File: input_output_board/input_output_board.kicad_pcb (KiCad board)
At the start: 2 copper layers, 150 x 50 mm, 24 parts, among them J1 Neutrik_NCJ6FA-H-0, J2 Neutrik_NCJ6FA-H-0, J3 Neutrik_NCJ6FA-H-0, J4 Neutrik_NCJ6FA-H-0, J5 Neutrik_NC3MAH, J6 Conn_02x05_Odd_Even, J7 Molex_SL_01x02_Male, J8 Molex_SL_01x02_Male, J9 Molex_SL_01x02_Male, K1 G6S-2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

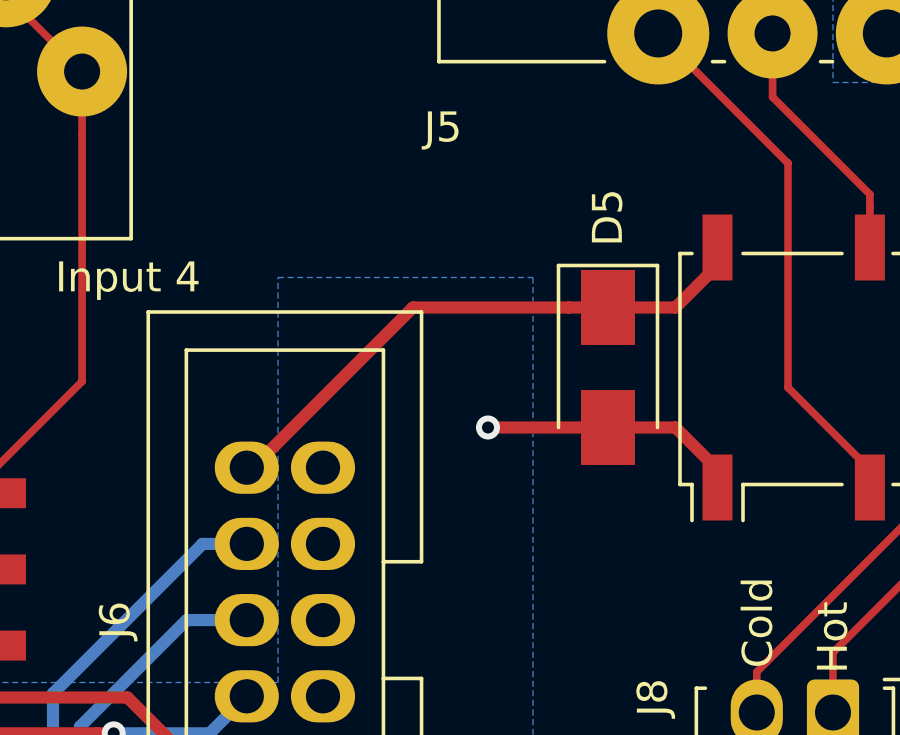
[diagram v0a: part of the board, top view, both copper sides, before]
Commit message: fix schematic/routing of headphone relay (reverse coil polarity)
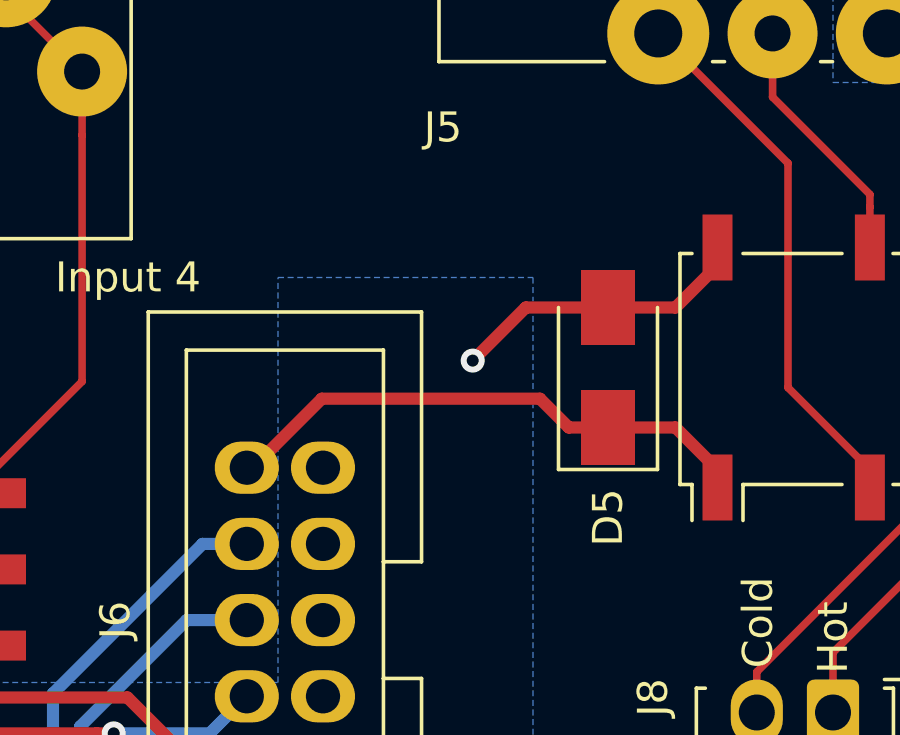
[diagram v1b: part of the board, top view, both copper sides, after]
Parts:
- turned D5 to 90 degrees
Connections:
- K5 pad 1: GNDRELAY -> /headphone_select
- K5 pad 12: /headphone_select -> GNDRELAY
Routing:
- net GNDRELAY: track 38.2 -> 39.4 mm
- net /headphone_select: track 19.3 -> 18.4 mm
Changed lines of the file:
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@@
     (thickness 1.6)
     (drawings 12)
-    (tracks 190)
+    (tracks 192)
     (zones 0)
     (modules 24)
@@
       (net 33 /main_hot))
     (pad 1 smd rect (at -4 -6.35 90) (size 2.2 1) (layers F.Cu F.Paste F.Mask)
-      (net 29 GNDRELAY))
+      (net 30 /headphone_select))
     (pad 10 smd rect (at 4 -1.27 90) (size 2.2 1) (layers F.Cu F.Paste F.Mask)
       (net 34 /main_cold))
     (pad 12 smd rect (at 4 -6.35 90) (size 2.2 1) (layers F.Cu F.Paste F.Mask)
-      (net 30 /headphone_select))
+      (net 29 GNDRELAY))
     (pad 4 smd rect (at -4 1.27 90) (size 2.2 1) (layers F.Cu F.Paste F.Mask)
       (net 15 /output_hot))
@@
   )
   (module Diode_SMD:D_SMA (layer F.Cu)
-    (at 178.5 128.5 270)
+    (at 178.5 128.5 90)
     (descr "Diode SMA (DO-214AC)")
     (tags "Diode SMA (DO-214AC)")
@@
       (effects (font (size 1 1) (thickness 0.15)))
     )
-    (pad 2 smd rect (at 2 0 270) (size 2.5 1.8) (layers F.Cu F.Paste F.Mask)
+    (pad 2 smd rect (at 2 0 90) (size 2.5 1.8) (layers F.Cu F.Paste F.Mask)
       (net 29 GNDRELAY))
-    (pad 1 smd rect (at -2 0 270) (size 2.5 1.8) (layers F.Cu F.Paste F.Mask)
+    (pad 1 smd rect (at -2 0 90) (size 2.5 1.8) (layers F.Cu F.Paste F.Mask)
       (net 30 /headphone_select))
     (model ${KISYS3DMOD}/Diode_SMD.3dshapes/D_SMA.wrl
@@
   (via (at 149.5 146.5) (size 0.8) (drill 0.4) (layers F.Cu B.Cu) (net 29))
   (segment (start 152 146.5) (end 149.5 146.5) (width 0.4064) (layer F.Cu) (net 29))
-  (segment (start 178.5 130.5) (end 174.5 130.5) (width 0.4064) (layer F.Cu) (net 29))
-  (via (at 174.5 130.5) (size 0.8) (drill 0.4) (layers F.Cu B.Cu) (net 29))
-  (segment (start 182.15 131.9) (end 182.15 132.5) (width 0.4064) (layer F.Cu) (net 29))
-  (segment (start 180.75 130.5) (end 182.15 131.9) (width 0.4064) (layer F.Cu) (net 29))
-  (segment (start 178.5 130.5) (end 180.75 130.5) (width 0.4064) (layer F.Cu) (net 29))
+  (segment (start 178.5 126.5) (end 175.76 126.5) (width 0.4064) (layer F.Cu) (net 29))
+  (via (at 173.99 128.27) (size 0.8) (drill 0.4) (layers F.Cu B.Cu) (net 29))
+  (segment (start 175.76 126.5) (end 173.99 128.27) (width 0.4064) (layer F.Cu) (net 29))
+  (segment (start 182.15 125.1) (end 182.15 124.5) (width 0.4064) (layer F.Cu) (net 29))
+  (segment (start 180.75 126.5) (end 182.15 125.1) (width 0.4064) (layer F.Cu) (net 29))
+  (segment (start 178.5 126.5) (end 180.75 126.5) (width 0.4064) (layer F.Cu) (net 29))
   (segment (start 166.46 131.38) (end 166.26 131.38) (width 0.4064) (layer B.Cu) (net 30))
-  (segment (start 177.1936 126.5) (end 178.5 126.5) (width 0.4064) (layer F.Cu) (net 30))
-  (segment (start 172 126.5) (end 177.1936 126.5) (width 0.4064) (layer F.Cu) (net 30))
-  (segment (start 166.66 131.84) (end 172 126.5) (width 0.4064) (layer F.Cu) (net 30))
-  (segment (start 166.46 131.84) (end 166.66 131.84) (width 0.4064) (layer F.Cu) (net 30))
-  (segment (start 182.15 125.1) (end 182.15 124.5) (width 0.4064) (layer F.Cu) (net 30))
-  (segment (start 180.75 126.5) (end 182.15 125.1) (width 0.4064) (layer F.Cu) (net 30))
-  (segment (start 178.5 126.5) (end 180.75 126.5) (width 0.4064) (layer F.Cu) (net 30))
+  (segment (start 177.1936 130.5) (end 176.2336 129.54) (width 0.4064) (layer F.Cu) (net 30))
+  (segment (start 178.5 130.5) (end 177.1936 130.5) (width 0.4064) (layer F.Cu) (net 30))
+  (segment (start 166.66 131.84) (end 166.46 131.84) (width 0.4064) (layer F.Cu) (net 30))
+  (segment (start 168.96 129.54) (end 166.66 131.84) (width 0.4064) (layer F.Cu) (net 30))
+  (segment (start 176.2336 129.54) (end 168.96 129.54) (width 0.4064) (layer F.Cu) (net 30))
+  (segment (start 182.15 131.9) (end 182.15 132.5) (width 0.4064) (layer F.Cu) (net 30))
+  (segment (start 180.75 130.5) (end 182.15 131.9) (width 0.4064) (layer F.Cu) (net 30))
+  (segment (start 178.5 130.5) (end 180.75 130.5) (width 0.4064) (layer F.Cu) (net 30))
   (segment (start 193.46 138.646) (end 191 136.186) (width 0.254) (layer F.Cu) (net 31))
   (segment (start 193.46 140) (end 193.46 138.646) (width 0.254) (layer F.Cu) (net 31))

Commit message: update sheet date, revision, and board silkscreen
Update sheet info/silk to give today's date and rev1
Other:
- board text added: "Input/Output Board rev1 Preamp 2019 G. Keeth 2019-10-13"
- board text removed: "Input/Output Board rev0 Preamp 2019 G. Keeth 2019-09-22"
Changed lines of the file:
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@@
   (title_block
     (title "Input/Output Board")
-    (date 2019-09-22)
-    (rev 0)
+    (date 2019-10-13)
+    (rev 1)
     (company "G. Keeth")
     (comment 1 "Preamp 2019")
@@
     (arrow2b (pts (xy 63.985 78.5) (xy 65.111504 77.913579)))
   )
-  (gr_text "Input/Output Board rev0\nPreamp 2019\nG. Keeth\n2019-09-22" (at 117.5 143.5) (layer B.SilkS)
+  (gr_text "Input/Output Board rev1\nPreamp 2019\nG. Keeth\n2019-10-13" (at 117.5 143.5) (layer B.SilkS)
     (effects (font (size 1 1) (thickness 0.15)) (justify left mirror))
   )

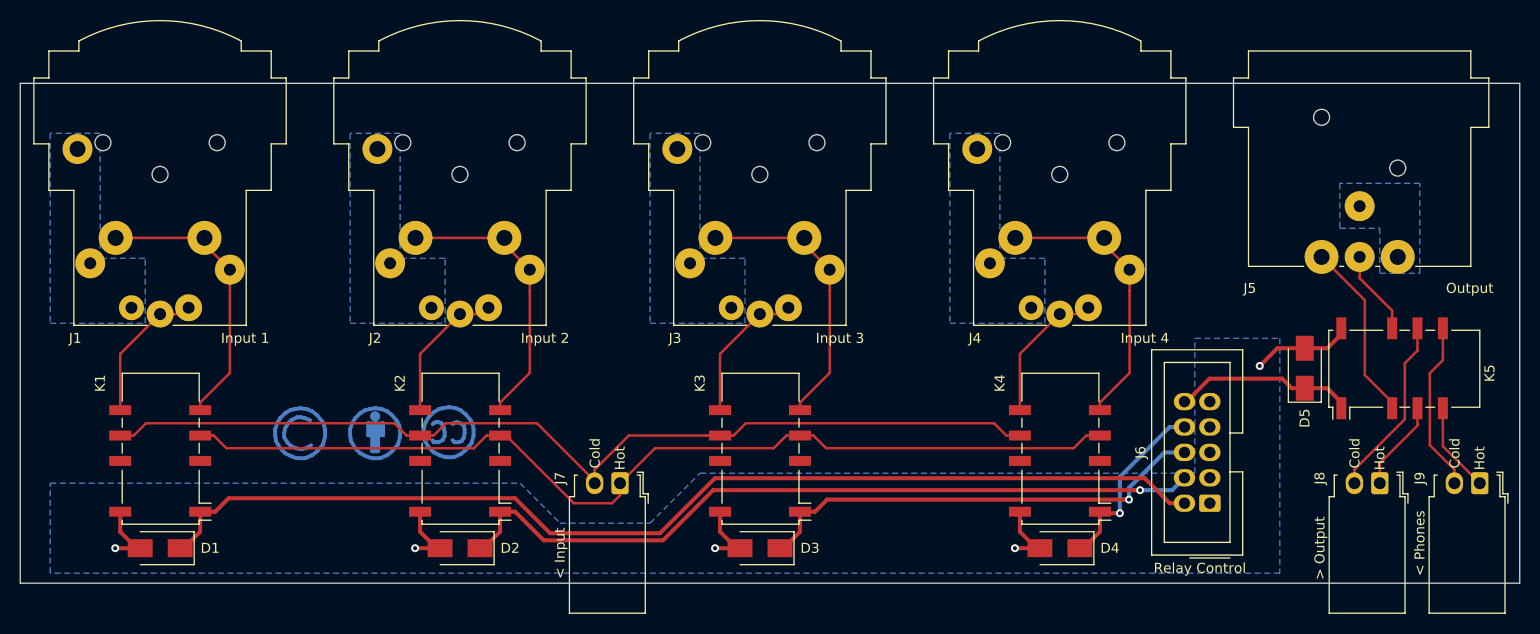
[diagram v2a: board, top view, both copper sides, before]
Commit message: update input output board to use a right-angle relay connector (requiring renumbering of connector pins)
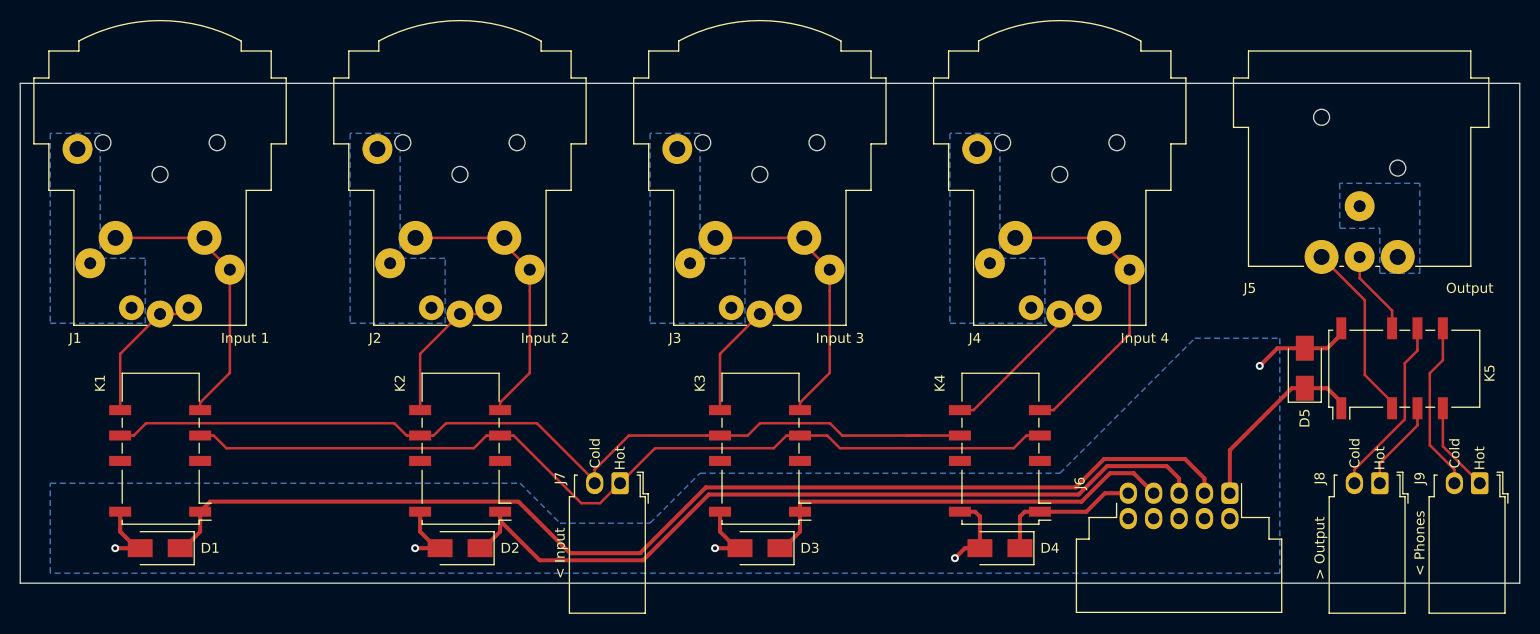
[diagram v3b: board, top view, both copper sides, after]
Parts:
- removed the REF** at (85.5, 135.0)
- removed the REF** at (78.0, 135.0)
- removed the REF** at (93.0, 135.0)
- added G***: LOGO, Symbol_CreativeCommons:CC-BY-SA_SolderMaskTop_Medium, B.Cu at (144.0, 143.5)
- J6: footprint Connector_Molex_C-Grid:Molex_C-Grid_70246-1001_2x05_P2.54mm_Vertical -> Connector_Molex_C-Grid:Molex_C-Grid_70247-10xx_2x05_P2.54mm_Horizontal
- moved REF** 40.0 mm to (125.5, 144.5)
- moved REF** 22.5 mm to (88.0, 143.0)
- moved D4 6.00 mm to (148.0, 146.5)
- moved K4 6.00 mm to (148.0, 136.5)
- moved J6 2.24 mm to (171.0, 141.0), turned to 270 degrees
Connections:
- J6 pad 1: GNDRELAY -> /headphone_select
- J6 pad 10: /headphone_select -> GNDRELAY
- J6 pad 2: /input1_select -> GNDRELAY
- J6 pad 3: GNDRELAY -> /input1_select
- J6 pad 4: /input2_select -> GNDRELAY
- J6 pad 5: GNDRELAY -> /input2_select
- J6 pad 6: /input3_select -> GNDRELAY
- J6 pad 7: GNDRELAY -> /input3_select
- J6 pad 8: /input4_select -> GNDRELAY
- J6 pad 9: GNDRELAY -> /input4_select
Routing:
- net /input_selected_hot: track 98.4 -> 91.7 mm
- net /input1_select: track 108.5 -> 113.9 mm
- net /input_selected_cold: track 97.9 -> 93.2 mm
- net /input4_select: track 19.1 -> 15.0 mm, vias 1 -> 0
- net /input2_select: track 76.9 -> 81.0 mm, vias 1 -> 0
- net /input3_select: track 46.5 -> 43.0 mm, vias 1 -> 0
- net /input4_hot: track 28.4 -> 31.7 mm
- net /input4_cold: track 14.4 -> 17.7 mm
- net /headphone_select: track 18.4 -> 19.2 mm
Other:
- board text added: "Input/Output Board rev2 Preamp 2019 G. Keeth 2019-12-15"
- board text removed: "Input/Output Board rev1 Preamp 2019 G. Keeth 2019-10-13"
